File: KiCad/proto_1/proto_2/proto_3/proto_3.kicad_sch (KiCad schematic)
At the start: 13 parts, among them J1 Screw_Terminal_01x02, J2 Screw_Terminal_01x02

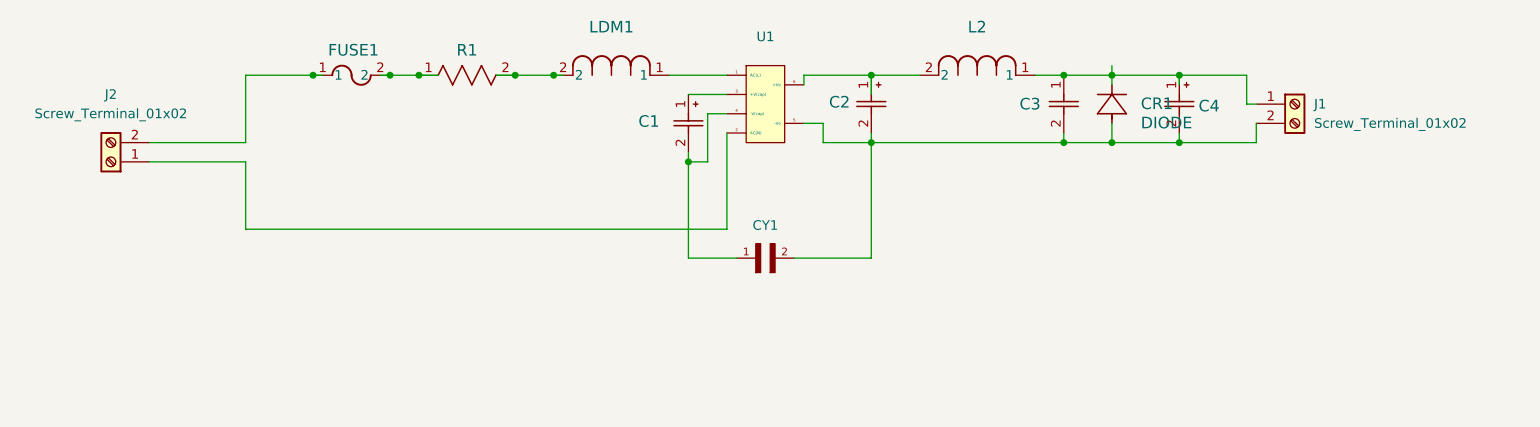
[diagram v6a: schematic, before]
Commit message: added 1x4 screw terminal for input and output voltage rails
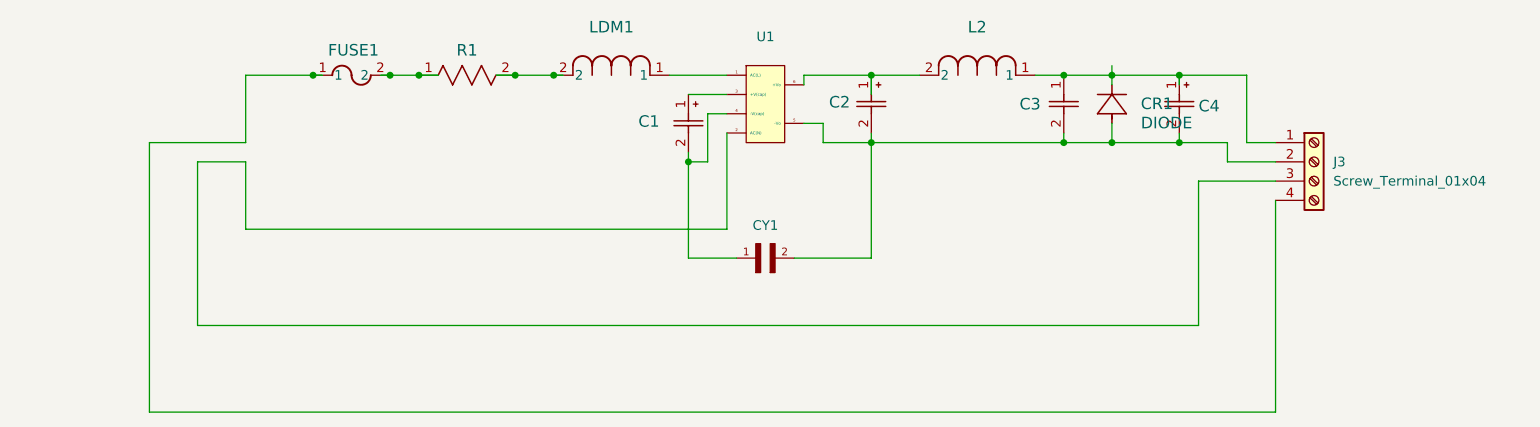
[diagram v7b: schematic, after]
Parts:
- removed J1, J2: Screw_Terminal_01x02, symbol Connector:Screw_Terminal_01x02
- added J3: Screw_Terminal_01x04, symbol Connector:Screw_Terminal_01x04
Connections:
- net at C3.1, C4.1, L2.1: now also J3.1 (Pin_1)
- net at C2.2, C3.2, C4.2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: now also J3.2 (Pin_2)
- net at U1.2 (AC(N)): now also J3.3 (Pin_3)
- net at FUSE1.1: now also J3.4 (Pin_4)
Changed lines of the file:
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@@
+	(wire
+		(pts
+			(xy 72.39 114.3) (xy 66.04 114.3)
+		)
+		(stroke
+			(width 0)
+			(type default)
+		)
+	)
 	(wire
 		(pts
@@
 	(wire
 		(pts
-			(xy 195.58 111.76) (xy 205.74 111.76)
+			(xy 201.93 111.76) (xy 201.93 114.3)
 		)
 		(stroke
@@
 	(wire
 		(pts
+			(xy 66.04 114.3) (xy 66.04 135.89)
+		)
+		(stroke
+			(width 0)
+			(type default)
+		)
+	)
+	(wire
+		(pts
 			(xy 176.53 102.87) (xy 180.34 102.87)
 		)
@@
 	(wire
 		(pts
+			(xy 195.58 111.76) (xy 201.93 111.76)
+		)
+		(stroke
+			(width 0)
+			(type default)
+		)
+	)
+	(wire
+		(pts
 			(xy 186.69 102.87) (xy 195.58 102.87)
 		)
@@
 	(wire
 		(pts
-			(xy 204.47 106.68) (xy 205.74 106.68)
+			(xy 198.12 135.89) (xy 198.12 116.84)
+		)
+		(stroke
+			(width 0)
+			(type default)
+		)
+	)
+	(wire
+		(pts
+			(xy 59.69 147.32) (xy 208.28 147.32)
+		)
+		(stroke
+			(width 0)
+			(type default)
+		)
+	)
+	(wire
+		(pts
+			(xy 204.47 111.76) (xy 208.28 111.76)
 		)
 		(stroke
@@
 	(wire
 		(pts
+			(xy 59.69 111.76) (xy 59.69 147.32)
+		)
+		(stroke
+			(width 0)
+			(type default)
+		)
+	)
+	(wire
+		(pts
 			(xy 130.81 127) (xy 130.81 114.3)
 		)
@@
 	(wire
 		(pts
+			(xy 198.12 116.84) (xy 208.28 116.84)
+		)
+		(stroke
+			(width 0)
+			(type default)
+		)
+	)
+	(wire
+		(pts
 			(xy 135.89 110.49) (xy 135.89 123.19)
 		)
@@
 	(wire
 		(pts
-			(xy 72.39 114.3) (xy 59.69 114.3)
+			(xy 66.04 135.89) (xy 198.12 135.89)
 		)
 		(stroke
@@
 	(wire
 		(pts
+			(xy 208.28 147.32) (xy 208.28 119.38)
+		)
+		(stroke
+			(width 0)
+			(type default)
+		)
+	)
+	(wire
+		(pts
 			(xy 180.34 102.87) (xy 186.69 102.87)
 		)
@@
 	(wire
 		(pts
+			(xy 201.93 114.3) (xy 208.28 114.3)
+		)
+		(stroke
+			(width 0)
+			(type default)
+		)
+	)
+	(wire
+		(pts
 			(xy 154.94 111.76) (xy 180.34 111.76)
 		)
@@
 	(wire
 		(pts
-			(xy 205.74 109.22) (xy 205.74 111.76)
-		)
-		(stroke
-			(width 0)
-			(type default)
-		)
-	)
-	(wire
-		(pts
 			(xy 97.79 102.87) (xy 95.25 102.87)
 		)
@@
 	(wire
 		(pts
-			(xy 204.47 102.87) (xy 204.47 106.68)
+			(xy 204.47 102.87) (xy 204.47 111.76)
 		)
 		(stroke
@@
 	)
 	(symbol
+		(lib_id "Connector:Screw_Terminal_01x04")
+		(at 213.36 114.3 0)
+		(unit 1)
+		(exclude_from_sim no)
+		(in_bom yes)
+		(on_board yes)
+		(dnp no)
+		(fields_autoplaced yes)
+		(property "Reference" "J3"
+			(at 215.9 114.2999 0)
+			(effects
+				(font
+					(size 1.27 1.27)
+				)
+				(justify left)
+			)
+		)
+		(property "Value" "Screw_Terminal_01x04"
+			(at 215.9 116.8399 0)
+			(effects
+				(font
+					(size 1.27 1.27)
+				)
+				(justify left)
+			)
+		)
+		(property "Footprint" ""
+			(at 213.36 114.3 0)
+			(effects
+				(font
+					(size 1.27 1.27)
+				)
+				(hide yes)
+			)
+		)
+		(property "Datasheet" "~"
+			(at 213.36 114.3 0)
+			(effects
+				(font
+					(size 1.27 1.27)
+				)
+				(hide yes)
+			)
+		)
+		(property "Description" "Generic screw terminal, single row, 01x04, script generated (kicad-library-utils/schlib/autogen/connector/)"
+			(at 213.36 114.3 0)
+			(effects
+				(font
+					(size 1.27 1.27)
+				)
+				(hide yes)
+			)
+		)
+		(pin "1"
+		)
+		(pin "4"
+		)
+		(pin "3"
+		)
+		(pin "2"
+		)
+		(instances
+			(project ""
+				(path "/3ba3c426-0aff-4728-abf4-4c9cd318aec8"
+					(reference "J3")
+					(unit 1)
+				)
+			)
+		)
+	)
+	(symbol
 		(lib_id "Capacitor-.1uf-50v:UFW1H0R1MDD1TA")
 		(at 195.58 102.87 270)
@@
 	)
 	(symbol
-		(lib_id "Connector:Screw_Terminal_01x02")
-		(at 54.61 114.3 180)
-		(unit 1)
-		(exclude_from_sim no)
-		(in_bom yes)
-		(on_board yes)
-		(dnp no)
-		(fields_autoplaced yes)
-		(property "Reference" "J2"
-			(at 54.61 105.41 0)
-			(effects
-				(font
-					(size 1.27 1.27)
-				)
-			)
-		)
-		(property "Value" "Screw_Terminal_01x02"
-			(at 54.61 107.95 0)
-			(effects
-				(font
-					(size 1.27 1.27)
-				)
-			)
-		)
-		(property "Footprint" ""
-			(at 54.61 114.3 0)
-			(effects
-				(font
-					(size 1.27 1.27)
-				)
-				(hide yes)
-			)
-		)
-		(property "Datasheet" "~"
-			(at 54.61 114.3 0)
-			(effects
-				(font
-					(size 1.27 1.27)
-				)
-				(hide yes)
-			)
-		)
-		(property "Description" "Generic screw terminal, single row, 01x02, script generated (kicad-library-utils/schlib/autogen/connector/)"
-			(at 54.61 114.3 0)
-			(effects
-				(font
-					(size 1.27 1.27)
-				)
-				(hide yes)
-			)
-		)
-		(pin "2"
-		)
-		(pin "1"
-		)
-		(instances
-			(project ""
-				(path "/3ba3c426-0aff-4728-abf4-4c9cd318aec8"
-					(reference "J2")
-					(unit 1)
-				)
-			)
-		)
-	)
-	(symbol
 		(lib_id "Capacitor-1nf-400V:DE2E3SA102MN3AY02F")
 		(at 139.7 127 0)
@@
 					(unit 1)
 				)
-			)
-		)
-	)
-	(symbol
-		(lib_id "Connector:Screw_Terminal_01x02")
-		(at 210.82 106.68 0)
-		(unit 1)
-		(exclude_from_sim no)
-		(in_bom yes)
-		(on_board yes)
-		(dnp no)
-		(fields_autoplaced yes)
-		(property "Reference" "J1"
-			(at 213.36 106.6799 0)
-			(effects
-				(font
-					(size 1.27 1.27)
-				)
-				(justify left)
-			)
-		)
-		(property "Value" "Screw_Terminal_01x02"
-			(at 213.36 109.2199 0)
-			(effects
-				(font
-					(size 1.27 1.27)
-				)
-				(justify left)
-			)
-		)
-		(property "Footprint" ""
-			(at 210.82 106.68 0)
-			(effects
-				(font
-					(size 1.27 1.27)
-				)
-				(hide yes)
-			)
-		)
-		(property "Datasheet" "~"
-			(at 210.82 106.68 0)
-			(effects
-				(font
-					(size 1.27 1.27)
-				)
-				(hide yes)
-			)
-		)
-		(property "Description" "Generic screw terminal, single row, 01x02, script generated (kicad-library-utils/schlib/autogen/connector/)"
-			(at 210.82 106.68 0)
-			(effects
-				(font
-					(size 1.27 1.27)
-				)
-				(hide yes)
-			)
-		)
-		(pin "1"
-		)
-		(pin "2"
-		)
-		(instances
-			(project ""
-				(path "/3ba3c426-0aff-4728-abf4-4c9cd318aec8"
-					(reference "J1")
-					(unit 1)
-				)

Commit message: added tvs diode and 4 port screw down block to schematic
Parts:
- removed J3: Screw_Terminal_01x04, symbol Connector:Screw_Terminal_01x04
- added J1: ~, stuff:screw_down_1x4, symbol 1x4_block_sym:691137710004
- CR1: footprint SMBJSeries_LTF -> stuff:SMBJ7.0A
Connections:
- net at C3.1, C4.1, L2.1: now also J1.1
- net at C2.2, C3.2, C4.2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: now also J1.2
- net at U1.2 (AC(N)): now also J1.3
- net at FUSE1.1: now also J1.4
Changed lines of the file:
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@@
-	)
-	(symbol
-		(lib_id "Connector:Screw_Terminal_01x04")
-		(at 213.36 114.3 0)
-		(unit 1)
-		(exclude_from_sim no)
-		(in_bom yes)
-		(on_board yes)
-		(dnp no)
-		(fields_autoplaced yes)
-		(property "Reference" "J3"
-			(at 215.9 114.2999 0)
-			(effects
-				(font
-					(size 1.27 1.27)
-				)
-				(justify left)
-			)
-		)
-		(property "Value" "Screw_Terminal_01x04"
-			(at 215.9 116.8399 0)
-			(effects
-				(font
-					(size 1.27 1.27)
-				)
-				(justify left)
-			)
-		)
-		(property "Footprint" ""
-			(at 213.36 114.3 0)
-			(effects
-				(font
-					(size 1.27 1.27)
-				)
-				(hide yes)
-			)
-		)
-		(property "Datasheet" "~"
-			(at 213.36 114.3 0)
-			(effects
-				(font
-					(size 1.27 1.27)
-				)
-				(hide yes)
-			)
-		)
-		(property "Description" "Generic screw terminal, single row, 01x04, script generated (kicad-library-utils/schlib/autogen/connector/)"
-			(at 213.36 114.3 0)
-			(effects
-				(font
-					(size 1.27 1.27)
-				)
-				(hide yes)
-			)
-		)
-		(pin "1"
-		)
-		(pin "4"
-		)
-		(pin "3"
-		)
-		(pin "2"
-		)
-		(instances
-			(project ""
-				(path "/3ba3c426-0aff-4728-abf4-4c9cd318aec8"
-					(reference "J3")
-					(unit 1)
-				)
-			)
-		)
 	)
 	(symbol
@@
 			)
 		)
-		(property "Footprint" "SMBJSeries_LTF"
+		(property "Footprint" "stuff:SMBJ7.0A"
 			(at 195.834 106.68 0)
 			(effects
@@
 					(unit 1)
 				)
+			)
+		)
+	)
+	(symbol
+		(lib_id "1x4_block_sym:691137710004")
+		(at 213.36 116.84 270)
+		(unit 1)
+		(exclude_from_sim no)
+		(in_bom yes)
+		(on_board yes)
+		(dnp no)
+		(fields_autoplaced yes)
+		(property "Reference" "J1"
+			(at 212.438 109.42 0)
+			(effects
+				(font
+					(size 1.27 1.27)
+				)
+				(justify right bottom)
+				(hide yes)
+			)
+		)
+		(property "Value" "~"
+			(at 214.63 115.57 90)
+			(effects
+				(font
+					(size 1.27 1.27)
+				)
+				(justify left)
+			)
+		)
+		(property "Footprint" "stuff:screw_down_1x4"
+			(at 213.36 116.84 0)
+			(effects
+				(font
+					(size 1.27 1.27)
+				)
+				(justify bottom)
+				(hide yes)
+			)
+		)
+		(property "Datasheet" ""
+			(at 213.36 116.84 0)
+			(effects
+				(font
+					(size 1.27 1.27)
+				)
+				(hide yes)
+			)
+		)
+		(property "Description" ""
+			(at 213.36 116.84 0)
+			(effects
+				(font
+					(size 1.27 1.27)
+				)
+				(hide yes)
+			)
+		)
+		(property "DigiKey_Part_Number" ""
+			(at 213.36 116.84 0)
+			(effects
+				(font
+					(size 1.27 1.27)
+				)
+				(justify bottom)
+				(hide yes)
+			)
+		)
+		(property "SnapEDA_Link" ""
+			(at 213.36 116.84 0)
+			(effects
+				(font
+					(size 1.27 1.27)
+				)
+				(justify bottom)
+				(hide yes)
+			)
+		)
+		(property "Description_1" ""
+			(at 213.36 116.84 0)
+			(effects
+				(font
+					(size 1.27 1.27)
+				)
+				(justify bottom)
+				(hide yes)
+			)
+		)
+		(property "MF" ""
+			(at 213.36 116.84 0)
+			(effects
+				(font
+					(size 1.27 1.27)
+				)
+				(justify bottom)
+				(hide yes)
+			)
+		)
+		(property "Package" ""
+			(at 213.36 116.84 0)
+			(effects
+				(font
+					(size 1.27 1.27)
+				)
+				(justify bottom)
+				(hide yes)
+			)
+		)
+		(property "Check_prices" ""
+			(at 213.36 116.84 0)
+			(effects
+				(font
+					(size 1.27 1.27)
+				)
+				(justify bottom)
+				(hide yes)
+			)
+		)
+		(property "MP" ""
+			(at 213.36 116.84 0)
+			(effects
+				(font
+					(size 1.27 1.27)
+				)
+				(justify bottom)
+				(hide yes)
+			)
+		)
+		(pin "1"
+		)
+		(pin "2"
+		)
+		(pin "4"
+		)
+		(pin "3"
+		)
+		(instances
+			(project ""
+				(path "/3ba3c426-0aff-4728-abf4-4c9cd318aec8"
+					(reference "J1")
+					(unit 1)
+				)
